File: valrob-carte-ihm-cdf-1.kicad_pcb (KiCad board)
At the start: 2 copper layers, 55 x 75 mm, 85 parts, among them J1 USB_C_Receptacle_USB2.0_14P, J2 Conn_01x02, J3 Conn_01x02, J4 Conn_01x04_Pin, J5 Conn_01x04_Pin, J6 Conn_01x04_Pin, SW1 SW_Push, SW2 SW_Push, SW3 SW_DIP_x04, SW4 SW_SPDT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

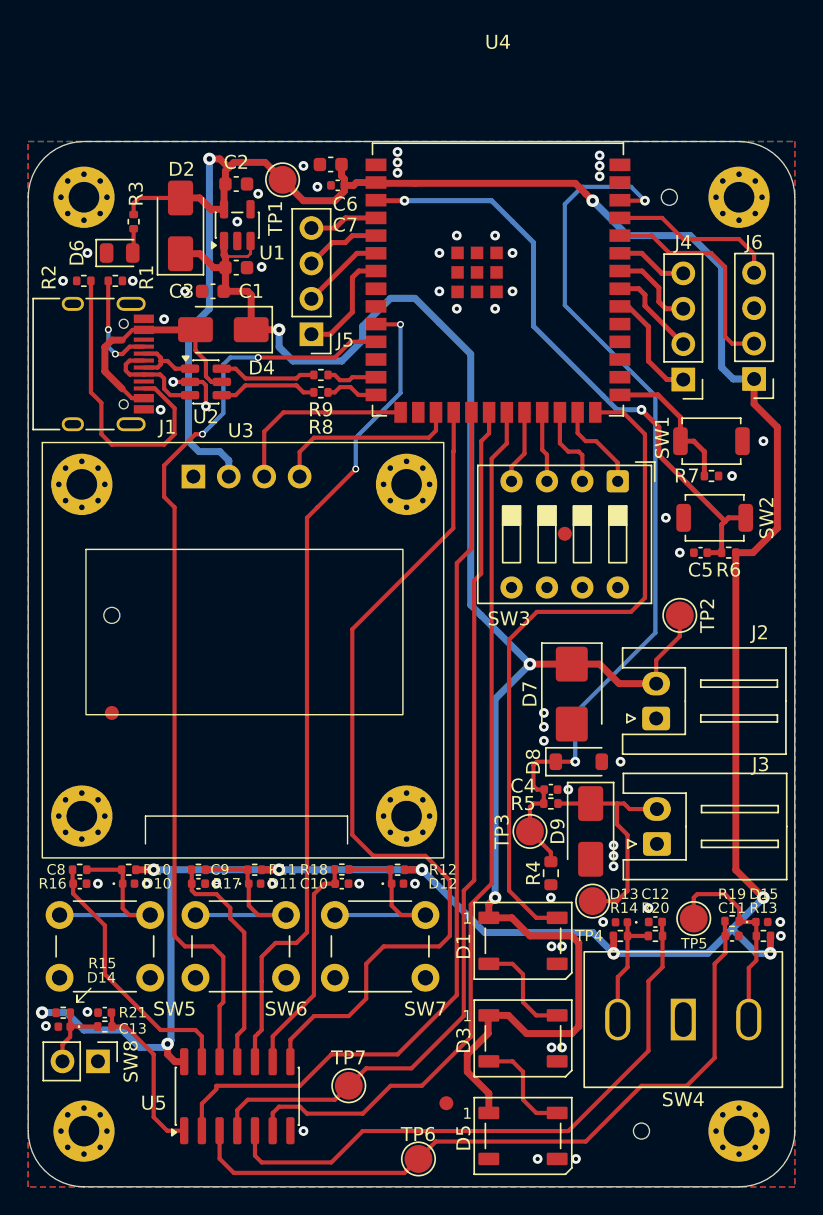
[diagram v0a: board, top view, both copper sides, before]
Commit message: pcb: add stitching vias
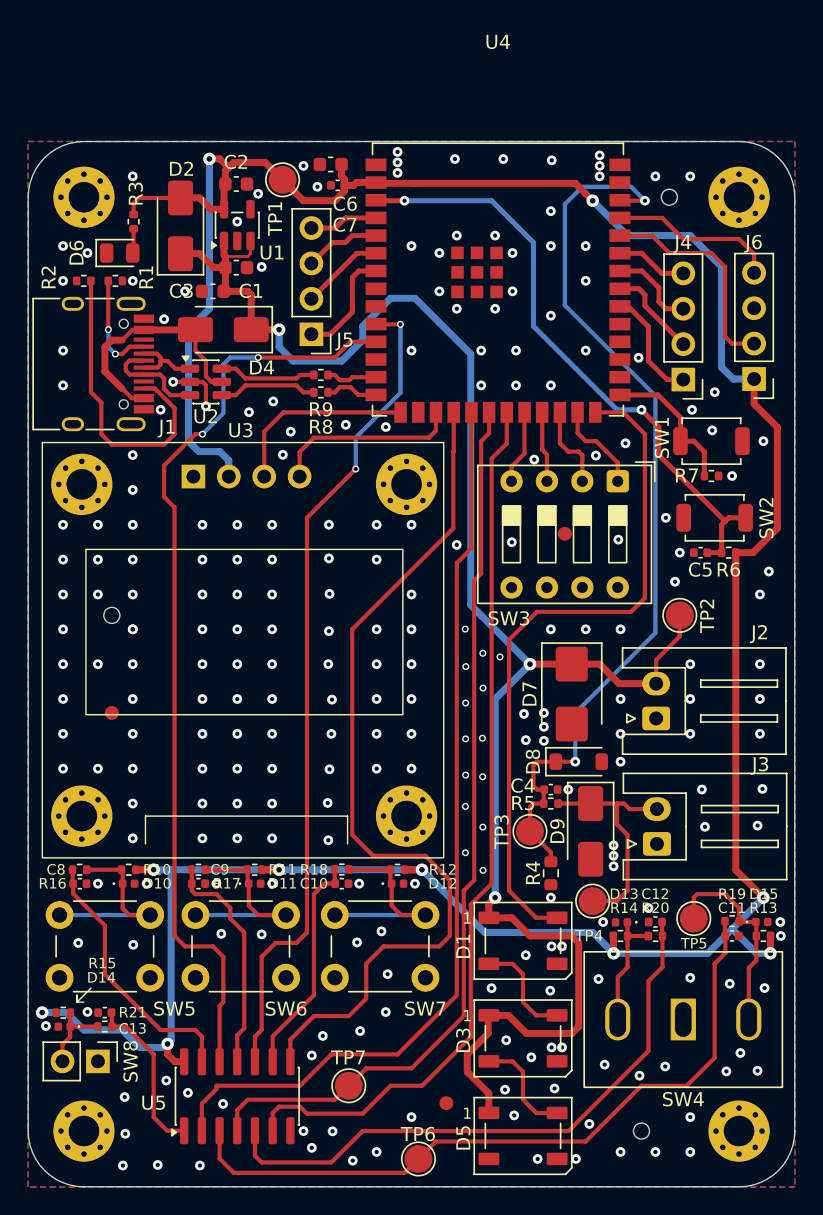
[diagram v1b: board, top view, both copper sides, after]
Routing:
- net GND: vias 59 -> 258

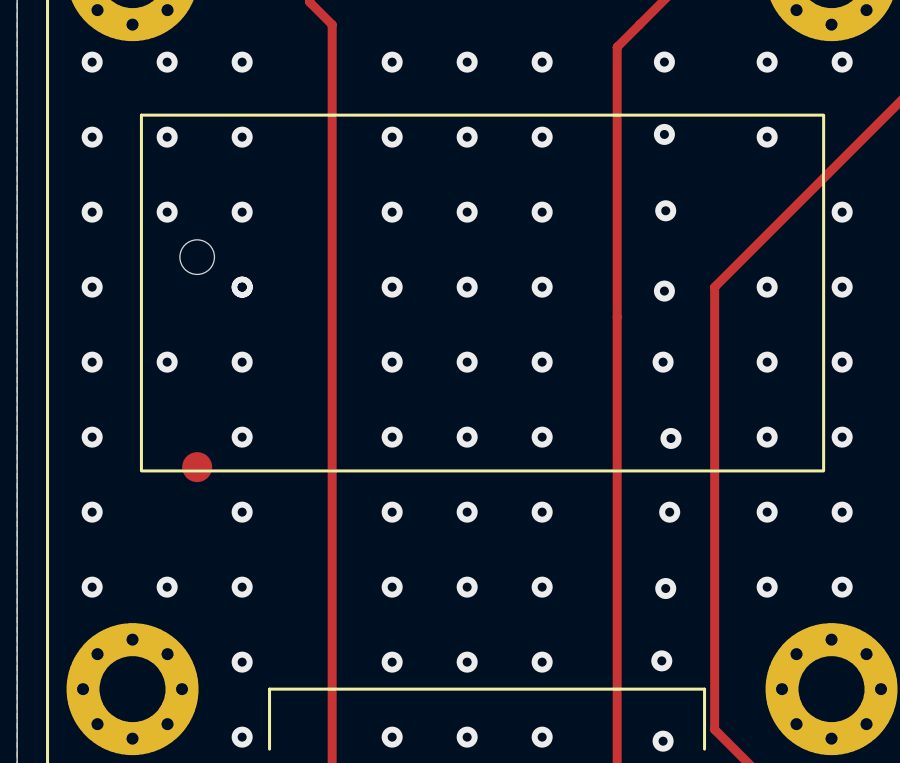
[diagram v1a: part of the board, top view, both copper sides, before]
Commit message: pcb(silkscreen): add company logo
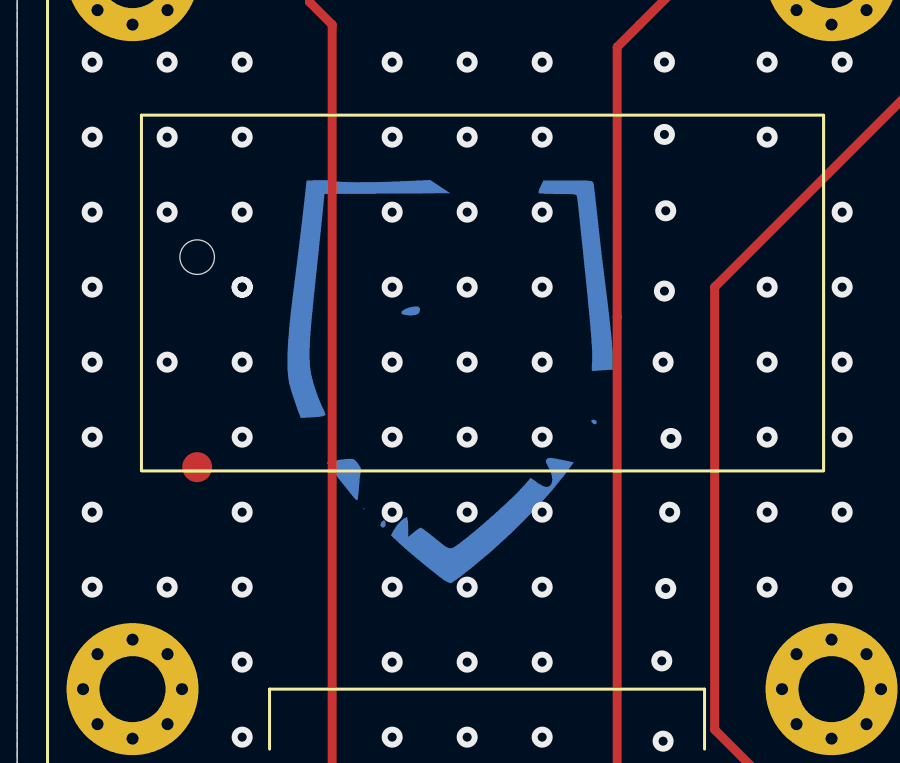
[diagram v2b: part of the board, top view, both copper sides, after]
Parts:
- added G*** (x3): LOGO, LOGO, B.Cu at (133.4, 104.8)

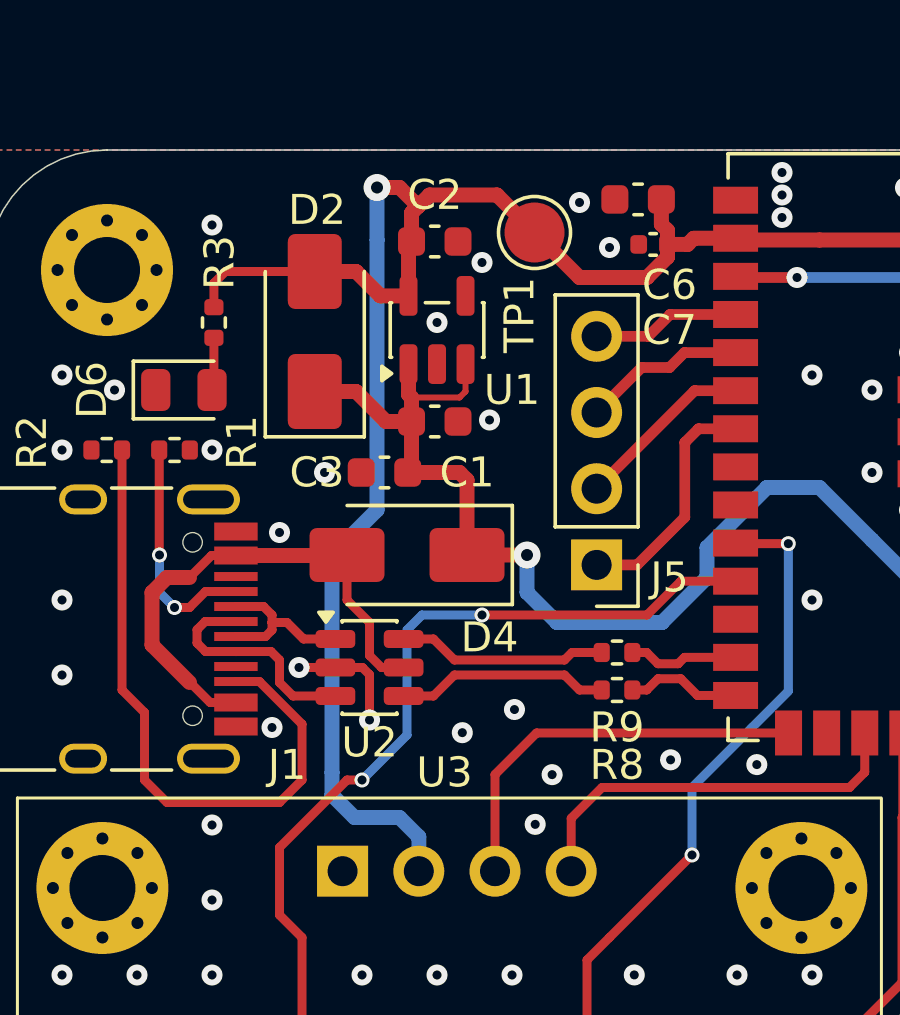
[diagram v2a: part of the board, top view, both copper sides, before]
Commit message: switch ST usb ESD to H5VU10U tvs diodes
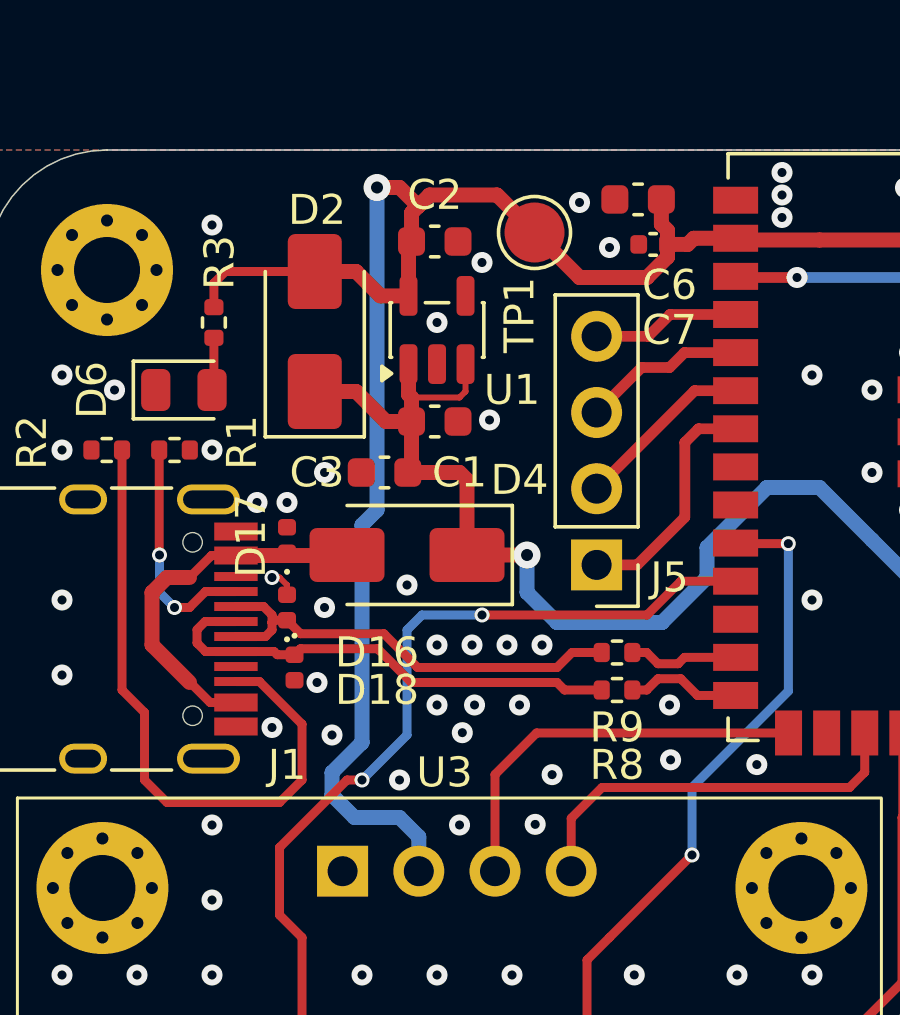
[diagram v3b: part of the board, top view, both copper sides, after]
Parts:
- removed U2: USBLC6-2SC6, Package_TO_SOT_SMD:SOT-23-6
- added D16: H5VU10U, Pers:Diode_DFN1006, F.Cu at (129.0, 83.2)
- added D17: H5VU10U, Pers:Diode_DFN1006, F.Cu at (129.0, 81.0)
- added D18: H5VU10U, Pers:Diode_DFN1006, F.Cu at (129.2, 85.2)
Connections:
- J1 pad A6: Net-(J1-D+-PadA6) -> /D+
- J1 pad A7: Net-(J1-D--PadA7) -> /D-
- J1 pad B6: Net-(J1-D+-PadA6) -> /D+
- J1 pad B7: Net-(J1-D--PadA7) -> /D-
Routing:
- net /D+: track 7.10 -> 16.2 mm
- net /D-: track 7.00 -> 15.0 mm
- net Net-(J1-D+-PadA6): track 7.64 -> 0.00 mm
- net Net-(J1-D--PadA7): track 5.45 -> 0.00 mm
- net VBUS: track 17.3 -> 12.4 mm
- net GND: track 3.96 -> 0.93 mm, vias 258 -> 271

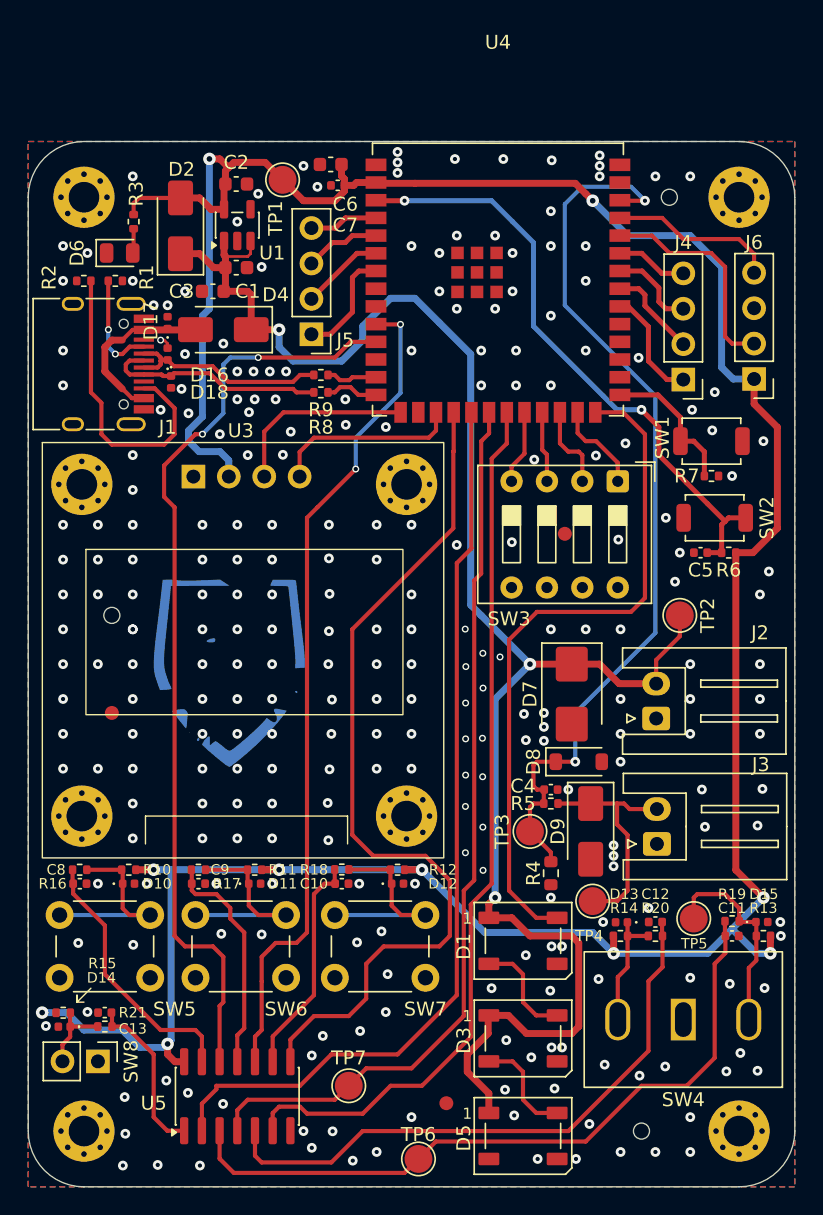
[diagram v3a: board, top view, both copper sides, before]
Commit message: pcb(silkscreen): improve user txt
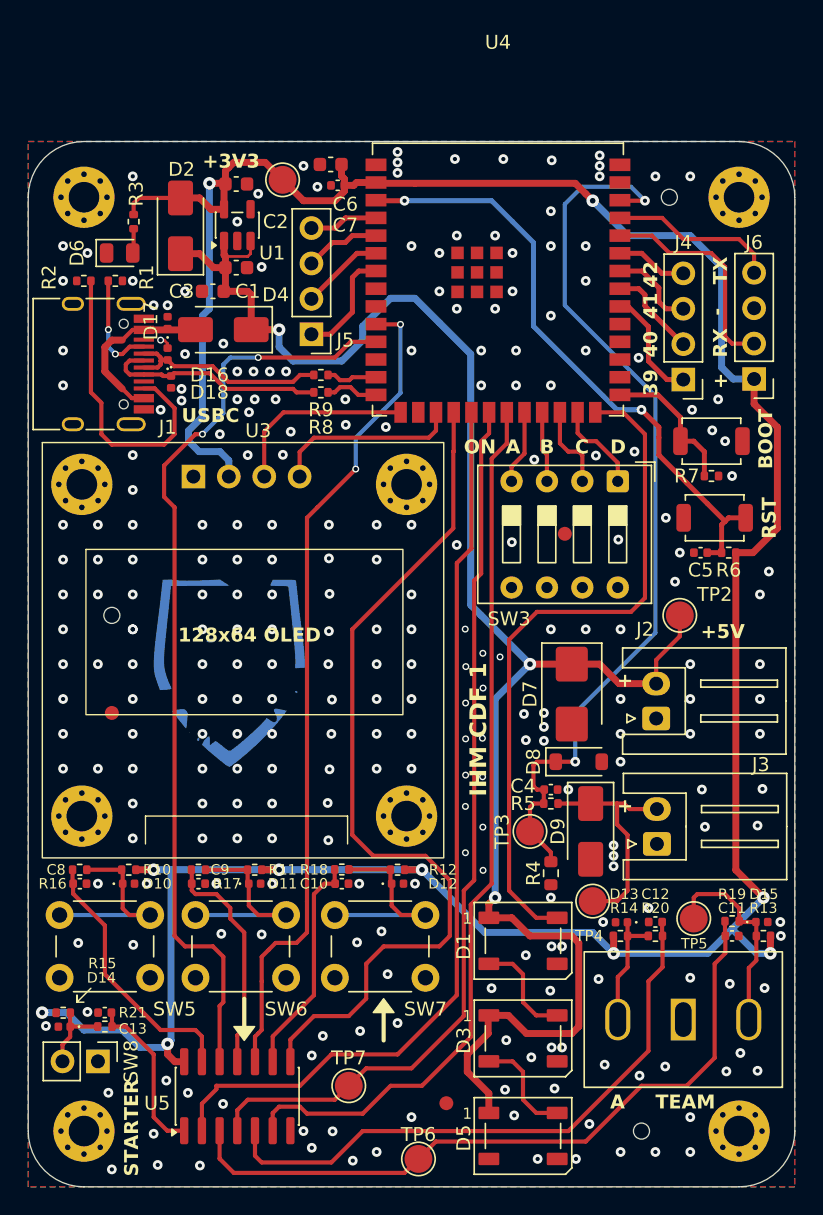
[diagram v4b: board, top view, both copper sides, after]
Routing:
- net +3V3: track 212.9 -> 210.7 mm
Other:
- board text added: "+"
- board text added: "+3V3"
- board text added: "+5V"
- board text added: "-"
- board text added: "128x64 OLED"
- board text added: "39"
- board text added: "40"
- board text added: "41"
- board text added: "42"
- board text added: "A"
- board text added: "B"
- board text added: "BOOT"
- board text added: "C"
- board text added: "D"
- board text added: "IHM CDF 1"
- board text added: "ON"
- board text added: "RST"
- board text added: "RX"
- board text added: "STARTER"
- board text added: "TEAM"
- board text added: "TX"
- board text added: "USBC"

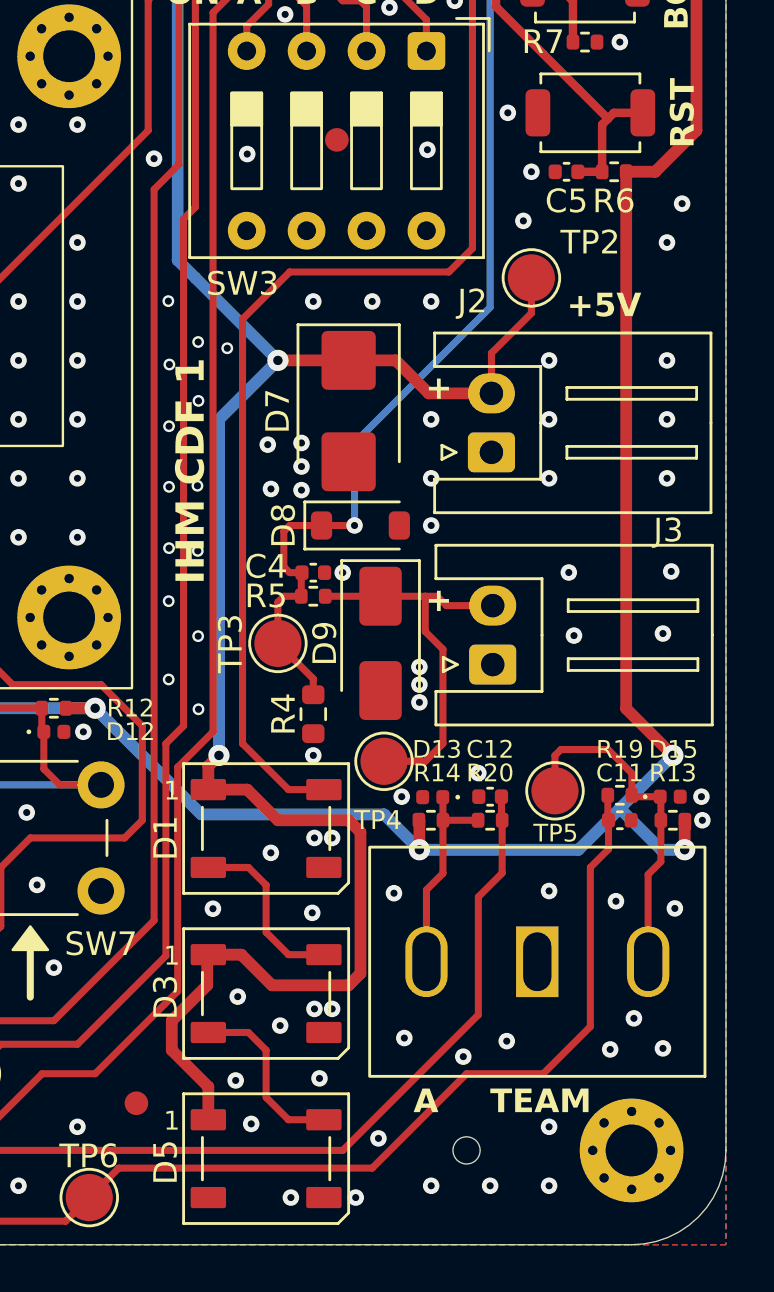
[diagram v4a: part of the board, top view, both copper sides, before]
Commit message: pcb(silkscreen): refine
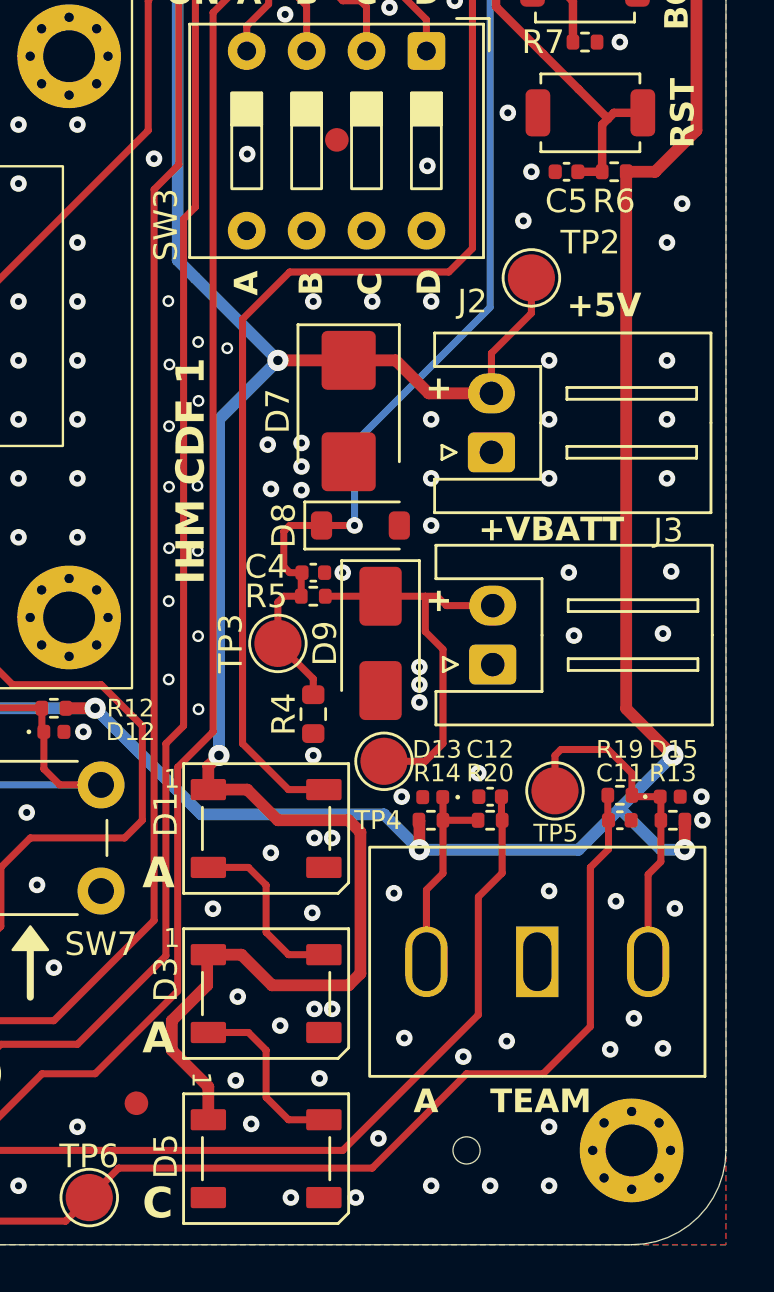
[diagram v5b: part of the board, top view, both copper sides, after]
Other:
- board text added: "+VBATT"
- board text added: "Carte IHM CDF 1"
- board text added: "DIPSWITCHES"
- board text added: "GPIOs"
- board text added: "JLCJLCJLCJLC"
- board text added: "R01"
- board text added: "UART"
- board text added: "Valrobotik 25-11"
